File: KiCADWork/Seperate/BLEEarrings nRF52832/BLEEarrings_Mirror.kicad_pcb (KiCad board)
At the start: 2 copper layers, 65.1 x 39.2 mm, 110 parts, among them J1 Screw_Terminal_01x01, J2 Screw_Terminal_01x02, J3 USB_C_Receptacle, SW1 TK-6580B-1, SW2 SW_DIP_x01, U1 MCP73831T-2ACI/OT, U2 XB6096I2SV, U3 NRF52833-QDAA-R7, Y1 XL7EL89CKI-111YLC-32M, Y1 locked, Y2 X161032768KLD2SI

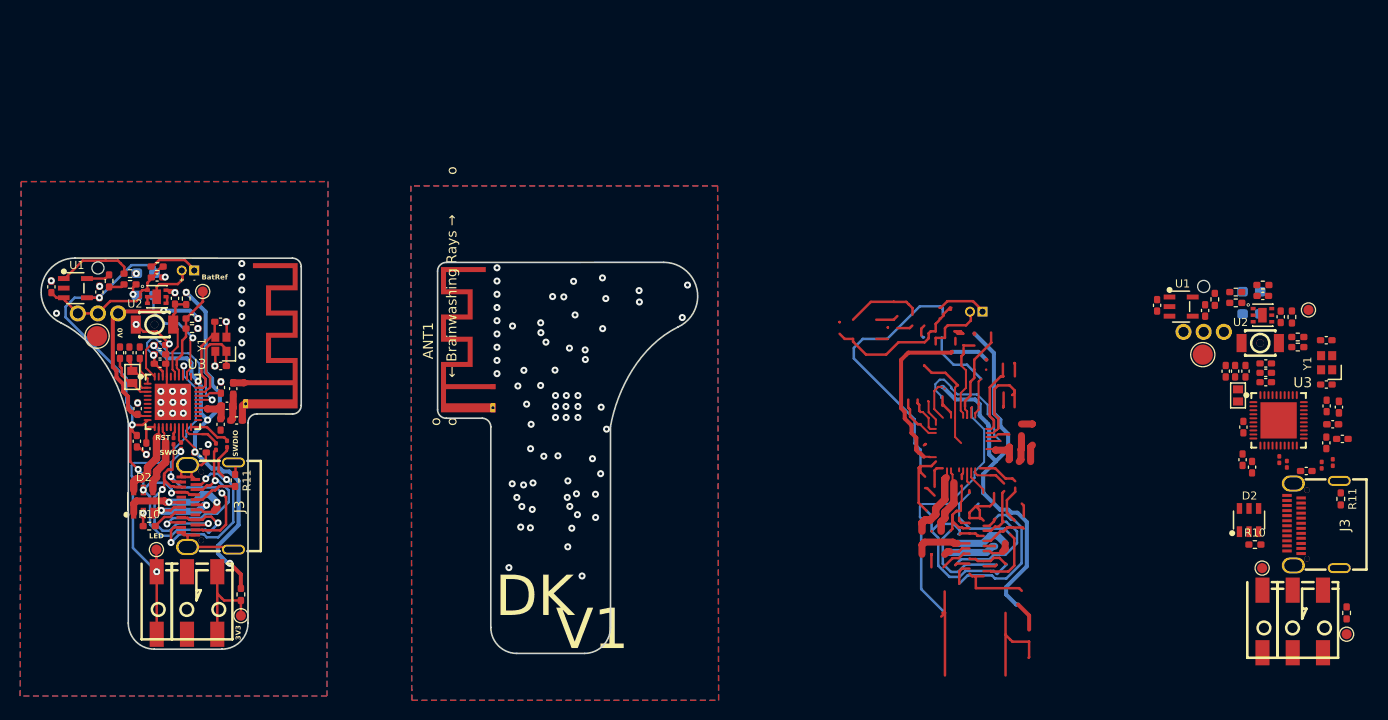
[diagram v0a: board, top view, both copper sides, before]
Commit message: Completing the combined layout
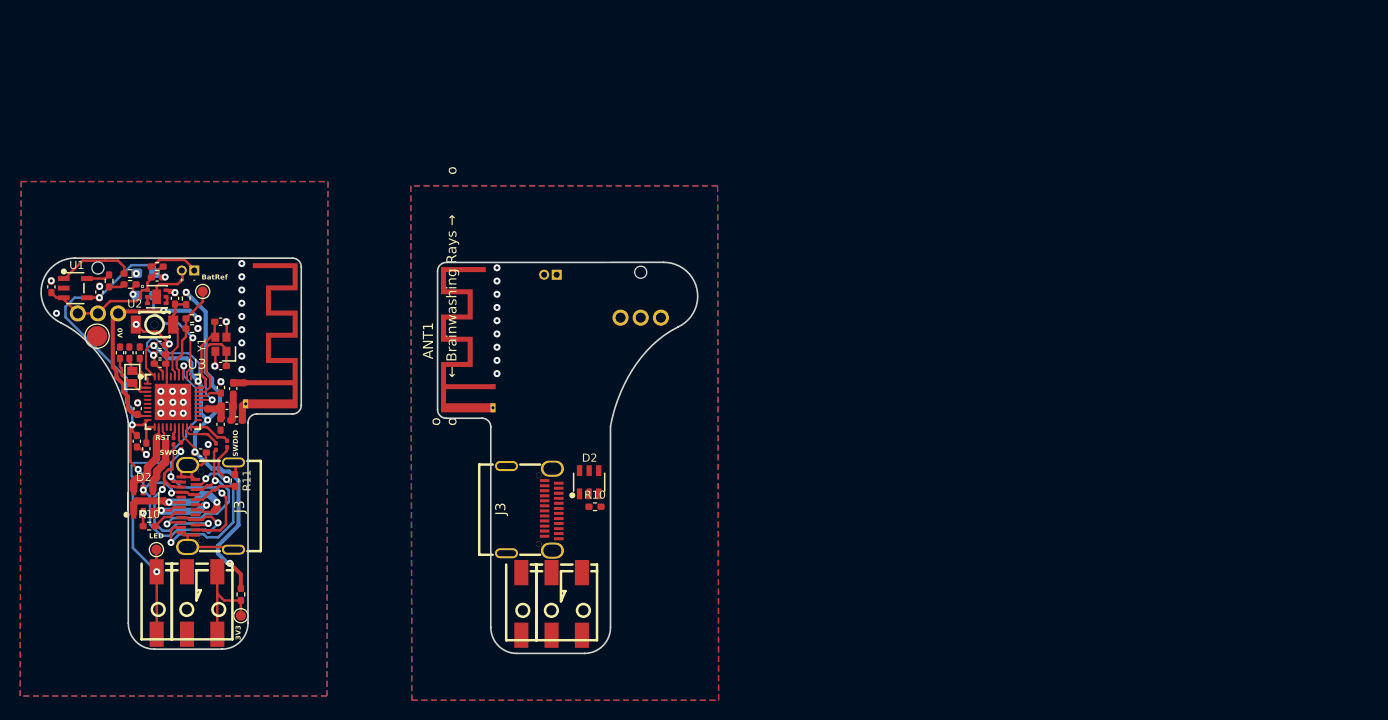
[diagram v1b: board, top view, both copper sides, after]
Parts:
- removed the C1 at (251.0, 52.5)
- removed the C10 at (248.7, 62.0)
- removed the C11 at (257.0, 56.7)
- removed the C12 at (248.8, 58.8)
- removed the C13 at (240.2, 46.7)
- removed the C14 at (252.5, 47.9)
- removed the C15 at (247.0, 53.3)
- removed the C16 at (247.9, 53.3)
- removed the C17 at (251.0, 53.4)
- removed the C18 at (250.7, 45.8)
- removed the C19 at (245.0, 47.2)
- removed the C2 at (249.0, 53.3)
- removed the C3 at (257.0, 54.6)
- removed the C4 at (257.0, 50.2)
- removed the C5 at (258.6, 60.0)
- removed the C6 at (255.0, 63.1)
- removed the C7 at (251.0, 54.4)
- removed the C8 at (257.0, 60.4)
- removed the C9 at (249.6, 62.8)
- removed the D1 at (249.6, 45.4)
- removed the D4 at (249.6, 47.6)
- removed the L1 at (257.6, 58.5)
- removed the L2 at (258.2, 56.8)
- removed the R1 at (248.0, 45.4)
- removed the R11 at (258.4, 65.9)
- removed the R12 at (248.0, 46.5)
- removed the R13 at (254.2, 49.9)
- removed the R14 at (254.2, 50.9)
- removed the R2 at (253.6, 47.9)
- removed the R3 at (250.7, 44.7)
- removed the R4 at (245.9, 46.1)
- removed the R5 at (252.3, 62.0)
- removed the R6 at (253.1, 62.5)
- removed the R7 at (257.6, 62.3)
- removed the R8 at (256.5, 62.6)
- removed the R9 at (259.0, 77.2)
- removed the SW2 at (250.4, 50.5)
- removed the TP10 at (250.6, 72.8)
- removed the TP11 at (259.0, 79.3)
- removed the TP16 at (244.7, 51.6)
- removed the TP9 at (255.2, 47.2)
- removed the U1 at (242.6, 46.9)
- removed the U2 at (250.7, 47.7)
- removed the U3 at (252.3, 58.1)
- removed the Y1 at (257.0, 52.4)
- removed the Y2 at (248.2, 55.7)
- moved J3 77.4 mm to (178.3, 67.0), turned to -90 degrees
- moved J1 73.5 mm to (175.7, 76.3)
- moved J2 73.5 mm to (181.7, 76.3)
- moved G*** 73.3 mm to (180.5, 60.6)
- moved R10 65.5 mm to (184.5, 66.7)
- moved D2 65.5 mm to (183.9, 64.3)
- moved SW1 55.8 mm to (189.0, 48.0)
- moved BT1 42.4 mm to (180.1, 43.7)
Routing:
- net BatRef: track 63.5 -> 9.65 mm, vias 2 -> 0
- net GND: track 89.1 -> 38.4 mm, vias 65 -> 41
- net /DSP/VBUS: track 100.3 -> 59.1 mm, vias 11 -> 6
- net NEO_LED: track 72.6 -> 36.3 mm, vias 3 -> 2
- net Net-(D2-I/O2-Pad3): track 44.6 -> 8.59 mm, vias 5 -> 2
- net SWDIO_L: track 44.2 -> 22.1 mm, vias 5 -> 3
- net +BATT: track 41.8 -> 20.9 mm, vias 4 -> 3
- net SWO_L: track 33.8 -> 16.9 mm, vias 6 -> 3
- net SWDCLK_L: track 33.8 -> 16.9 mm, vias 4 -> 2
- net /Power/VBAT: track 29.7 -> 14.9 mm
- net Net-(D2-I/O1-Pad1): track 28.4 -> 14.2 mm, vias 4 -> 2
- net LED_A: track 21.2 -> 10.6 mm
- net Net-(J2-Pin_1): track 20.9 -> 10.4 mm, vias 1 -> 0
- net +3V3: track 64.0 -> 54.1 mm, vias 11 -> 6
- net Net-(U3-XC1): track 19.2 -> 9.58 mm
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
